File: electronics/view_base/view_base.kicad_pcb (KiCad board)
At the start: 2 copper layers, 81.2 x 81.2 mm, 96 parts, among them J1 BLDC, J2 USB_C_Receptacle_USB2.0, J3 LCD, J4 A, J5 B, Q1 MMBT4403, Q2 UMH3N, U1 MT6701-CT, U2 T-Micro32_Plus, U3 CH340C, U4 HX711, U5 TMC6300, U6 AP2114HA-3.3, U7 SN74LV1T34DBV, U8 VEML7700

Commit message: Generate merged BOM (#15)
Also add more bom-only items to the schematic
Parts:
- added Z10: BLDCMotor, BOM_Only:bom_only_no_pin, F.Cu at (121.9, 71.8)
- added Z6: RotorScrew (BOM-only), BOM_Only:bom_only_no_pin, F.Cu at (120.4, 71.8)
- added Z7: RotorScrew (BOM-only), BOM_Only:bom_only_no_pin, F.Cu at (121.9, 71.8)
- added Z8: RotorScrew (BOM-only), BOM_Only:bom_only_no_pin, F.Cu at (123.4, 71.8)
- added Z9: WatchGlass39.5mm, BOM_Only:bom_only_no_pin, F.Cu at (120.4, 71.8)

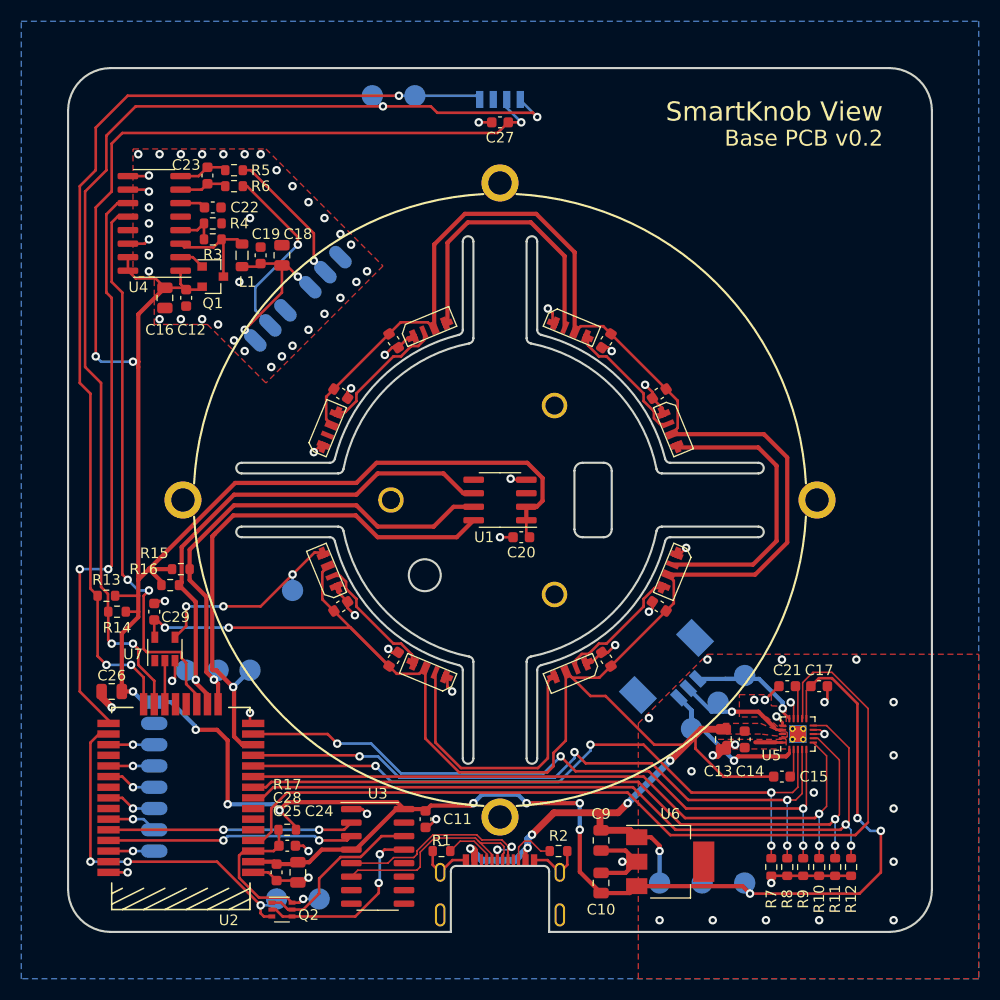
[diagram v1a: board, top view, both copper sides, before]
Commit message: Add alignment holes, update board outline - shorter slots
Fixes #7
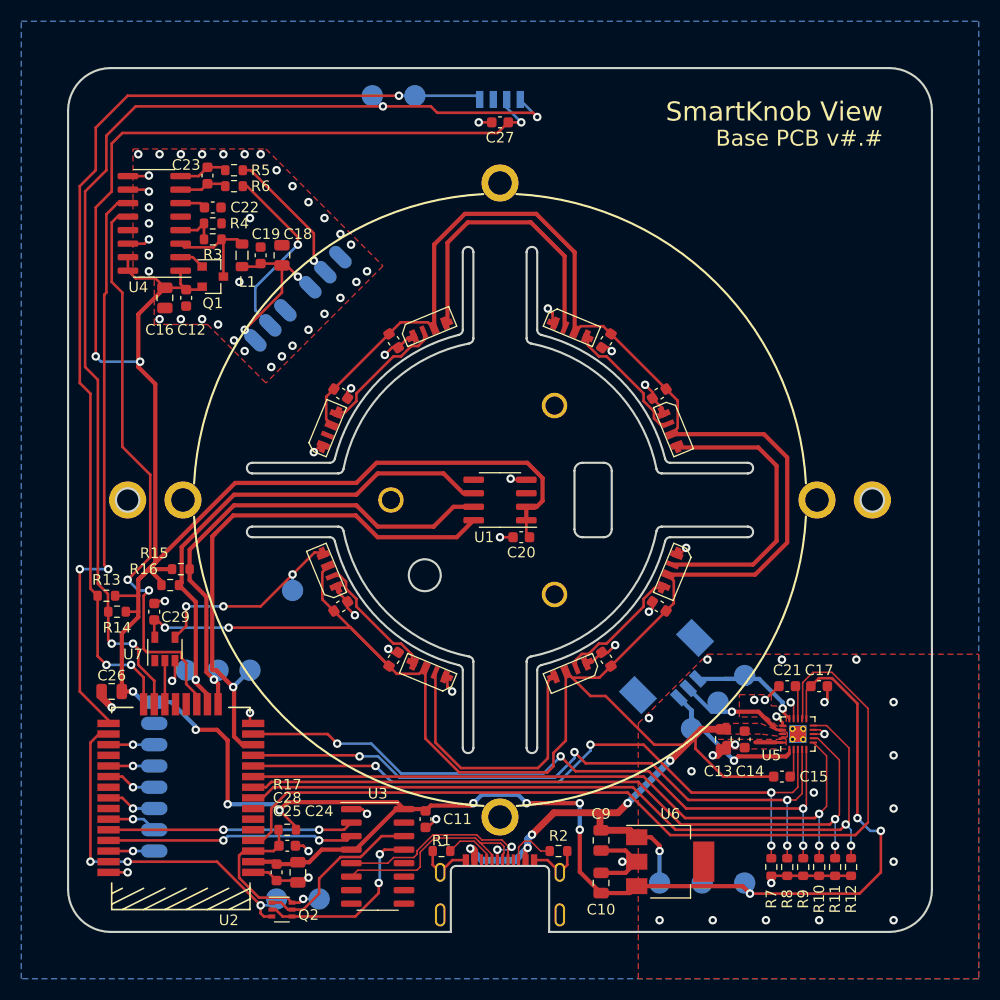
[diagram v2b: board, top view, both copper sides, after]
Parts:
- added H8: AlignmentHole, Holes:MountingHole_2.2mm_M2_ISO7380_Pad_NonVirtual, F.Cu at (135.0, 100.0)
- added H9: AlignmentHole, Holes:MountingHole_2.2mm_M2_ISO7380_Pad_NonVirtual, F.Cu at (65.0, 100.0)
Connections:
- D8 pad 3: (no net) -> Net-(D8-Pad3)
- H1 pad 1: (no net) -> Net-(H1-Pad1)
- H2 pad 1: (no net) -> Net-(H2-Pad1)
- H3 pad 1: (no net) -> Net-(H3-Pad1)
- H4 pad 1: (no net) -> Net-(H4-Pad1)
- H5 pad 1: (no net) -> Net-(H5-Pad1)
- H6 pad 1: (no net) -> Net-(H6-Pad1)
- H7 pad 1: (no net) -> Net-(H7-Pad1)
- J2 pad A8: (no net) -> Net-(J2-PadA8)
- J2 pad B8: (no net) -> Net-(J2-PadB8)
- U1 pad 3: (no net) -> Net-(U1-Pad3)
- U1 pad 5: (no net) -> Net-(U1-Pad5)
- U2 pad 19: (no net) -> Net-(U2-Pad19)
- U2 pad 20: (no net) -> Net-(U2-Pad20)
- U2 pad 27: (no net) -> Net-(U2-Pad27)
- U2 pad 30: (no net) -> Net-(U2-Pad30)
- U2 pad 32: (no net) -> Net-(U2-Pad32)
- U2 pad 37: (no net) -> Net-(U2-Pad37)
- U2 pad 5: (no net) -> Net-(U2-Pad5)
- U2 pad 6: (no net) -> Net-(U2-Pad6)
- U2 pad 7: (no net) -> Net-(U2-Pad7)
- U3 pad 10: (no net) -> Net-(U3-Pad10)
- U3 pad 11: (no net) -> Net-(U3-Pad11)
- U3 pad 12: (no net) -> Net-(U3-Pad12)
- U3 pad 15: (no net) -> Net-(U3-Pad15)
- U3 pad 7: (no net) -> Net-(U3-Pad7)
- U3 pad 8: (no net) -> Net-(U3-Pad8)
- U3 pad 9: (no net) -> Net-(U3-Pad9)
- U4 pad 13: (no net) -> Net-(U4-Pad13)
- U5 pad 19: (no net) -> Net-(U5-Pad19)
- U7 pad 1: (no net) -> Net-(U7-Pad1)
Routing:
- net /STRAIN_DO: track 53.5 -> 55.3 mm
- net +3V3: track 312.9 -> 314.6 mm
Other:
- outline, holes or cut-outs redrawn
- board text added: "Base PCB v#.#"
- board text removed: "Base PCB v0.2"

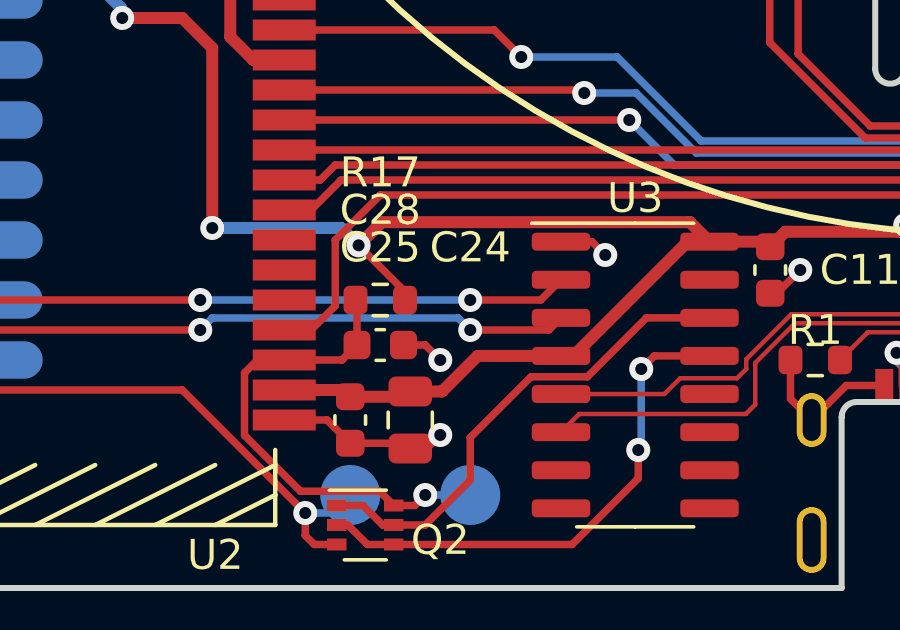
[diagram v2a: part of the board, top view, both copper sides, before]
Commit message: Add testpoints for RX and TX
Updates #14
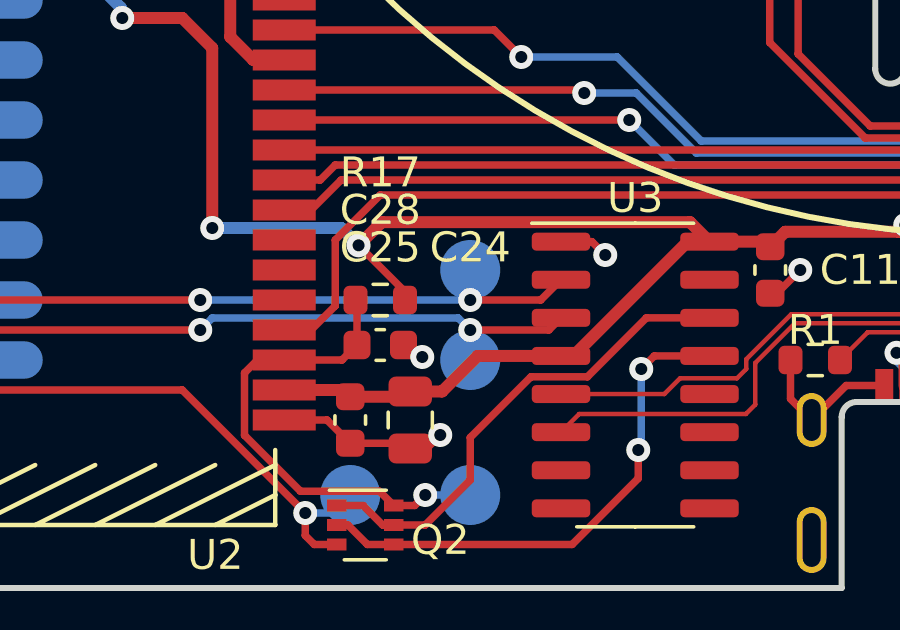
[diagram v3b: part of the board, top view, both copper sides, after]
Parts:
- added TP15: TX, Modified:TestPoint_Pad_D2.0mm_ValueSilk, B.Cu at (83.0, 133.0)
- added TP16: RX, Modified:TestPoint_Pad_D2.0mm_ValueSilk, B.Cu at (83.0, 130.0)
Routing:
- net GND: track 92.8 -> 92.2 mm
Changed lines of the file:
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@@
     (tracks 918)
     (zones 0)
-    (modules 103)
+    (modules 105)
     (nets 90)
   )
@@
   (layers
     (0 F.Cu signal)
-    (31 B.Cu signal)
+    (31 B.Cu signal hide)
     (32 B.Adhes user)
     (33 F.Adhes user)
@@
   )
   (setup
-    (last_trace_width 0.15)
+    (last_trace_width 0.25)
     (user_trace_width 0.25)
     (user_trace_width 0.4)
@@
     (add_net "Net-(U7-Pad1)")
   )
+  (module Modified:TestPoint_Pad_D2.0mm_ValueSilk (layer B.Cu)
+    (at 83 130 180)
+    (descr "SMD pad as test Point, diameter 2.0mm")
+    (tags "test point SMD pad")
+    (attr virtual)
+    (fp_text reference TP16 (at 0 1.998) (layer B.SilkS) hide
+      (effects (font (size 1 1) (thickness 0.15)) (justify mirror))
+    )
+    (fp_text value RX (at 0 -2.05) (layer B.Fab) hide
+      (effects (font (size 1 1) (thickness 0.15)) (justify mirror))
+    )
+    (fp_text user %V (at -2.5 0) (layer B.SilkS)
+      (effects (font (size 1 1) (thickness 0.15)) (justify mirror))
+    )
+    (fp_text user %R (at 0 2) (layer B.Fab)
+      (effects (font (size 1 1) (thickness 0.15)) (justify mirror))
+    )
+    (fp_circle (center 0 0) (end 0 -1.2) (layer B.SilkS) (width 0.12))
+    (fp_circle (center 0 0) (end 1.5 0) (layer B.CrtYd) (width 0.05))
+    (pad 1 smd circle (at 0 0 180) (size 2 2) (layers B.Cu B.Mask)
+      (net 34 /USB_SERIAL_TXO))
+  )
+  (module Modified:TestPoint_Pad_D2.0mm_ValueSilk (layer B.Cu)
+    (at 83 133 180)
+    (descr "SMD pad as test Point, diameter 2.0mm")
+    (tags "test point SMD pad")
+    (attr virtual)
+    (fp_text reference TP15 (at 0 1.998) (layer B.SilkS) hide
+      (effects (font (size 1 1) (thickness 0.15)) (justify mirror))
+    )
+    (fp_text value TX (at 0 -2.05) (layer B.Fab) hide
+      (effects (font (size 1 1) (thickness 0.15)) (justify mirror))
+    )
+    (fp_text user %V (at -2.5 0) (layer B.SilkS)
+      (effects (font (size 1 1) (thickness 0.15)) (justify mirror))
+    )
+    (fp_text user %R (at 0 2) (layer B.Fab)
+      (effects (font (size 1 1) (thickness 0.15)) (justify mirror))
+    )
+    (fp_circle (center 0 0) (end 0 -1.2) (layer B.SilkS) (width 0.12))
+    (fp_circle (center 0 0) (end 1.5 0) (layer B.CrtYd) (width 0.05))
+    (pad 1 smd circle (at 0 0 180) (size 2 2) (layers B.Cu B.Mask)
+      (net 33 /USB_SERIAL_RXI))
+  )
   (module view_custom:ViewKeepouts3d (layer F.Cu)
     (at 100 100)
@@
     (effects (font (size 1 1) (thickness 0.15)) (justify left mirror))
   )
-  (gr_text Display (at 75 132.5) (layer B.SilkS)
+  (gr_text Display (at 75 127) (layer B.SilkS)
     (effects (font (size 2 2) (thickness 0.3)) (justify mirror))
   )
@@
     (effects (font (size 2 2) (thickness 0.3)) (justify mirror))
   )
-  (gr_line (start 74 126) (end 71.5 126) (layer B.SilkS) (width 1))
-  (gr_line (start 91 109) (end 74 126) (layer B.SilkS) (width 1))
+  (gr_line (start 75.5 124.5) (end 71.5 124.5) (layer B.SilkS) (width 1))
+  (gr_line (start 91 109) (end 75.5 124.5) (layer B.SilkS) (width 1))
   (gr_line (start 112 96) (end 109.5 93.5) (layer B.SilkS) (width 1))
   (gr_line (start 109.5 93.5) (end 96 93.5) (layer B.SilkS) (width 1))
@@
   (segment (start 82.938698 95.061302) (end 82.5 95.5) (width 0.25) (layer F.Cu) (net 1))
   (segment (start 83.374289 95.061302) (end 82.938698 95.061302) (width 0.25) (layer F.Cu) (net 1))
-  (via (at 82 133) (size 0.8) (drill 0.4) (layers F.Cu B.Cu) (net 1))
-  (segment (start 81.5 132.5) (end 82 133) (width 0.25) (layer F.Cu) (net 1))
-  (segment (start 80.775 132.5) (end 81.5 132.5) (width 0.25) (layer F.Cu) (net 1))
   (segment (start 111.8 132.95) (end 112.85 134) (width 0.4) (layer F.Cu) (net 1))
   (segment (start 109.5 132.95) (end 111.8 132.95) (width 0.4) (layer F.Cu) (net 1))
@@
   (via (at 111.5 134) (size 0.8) (drill 0.4) (layers F.Cu B.Cu) (net 1))
   (segment (start 112.85 134) (end 111.5 134) (width 0.4) (layer F.Cu) (net 1))
+  (segment (start 81.000001 132.500001) (end 81.4 132.9) (width 0.25) (layer F.Cu) (net 1))
+  (segment (start 80.775 132.5) (end 81.000001 132.500001) (width 0.25) (layer F.Cu) (net 1))
+  (via (at 81.4 132.9) (size 0.8) (drill 0.4) (layers F.Cu B.Cu) (net 1))
   (segment (start 106.777719 116.701859) (end 109.339909 116.701859) (width 0.25) (layer F.Cu) (net 2))
   (segment (start 106.185237 116.109377) (end 106.777719 116.701859) (width 0.25) (layer F.Cu) (net 2) (status 10))
